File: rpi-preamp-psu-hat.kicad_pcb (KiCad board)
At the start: 2 copper layers, 41.9 x 55.9 mm, 20 parts, among them J1 Conn_02x20_Odd_Even, U1 NMH0515SC, U2 MC7809CTG

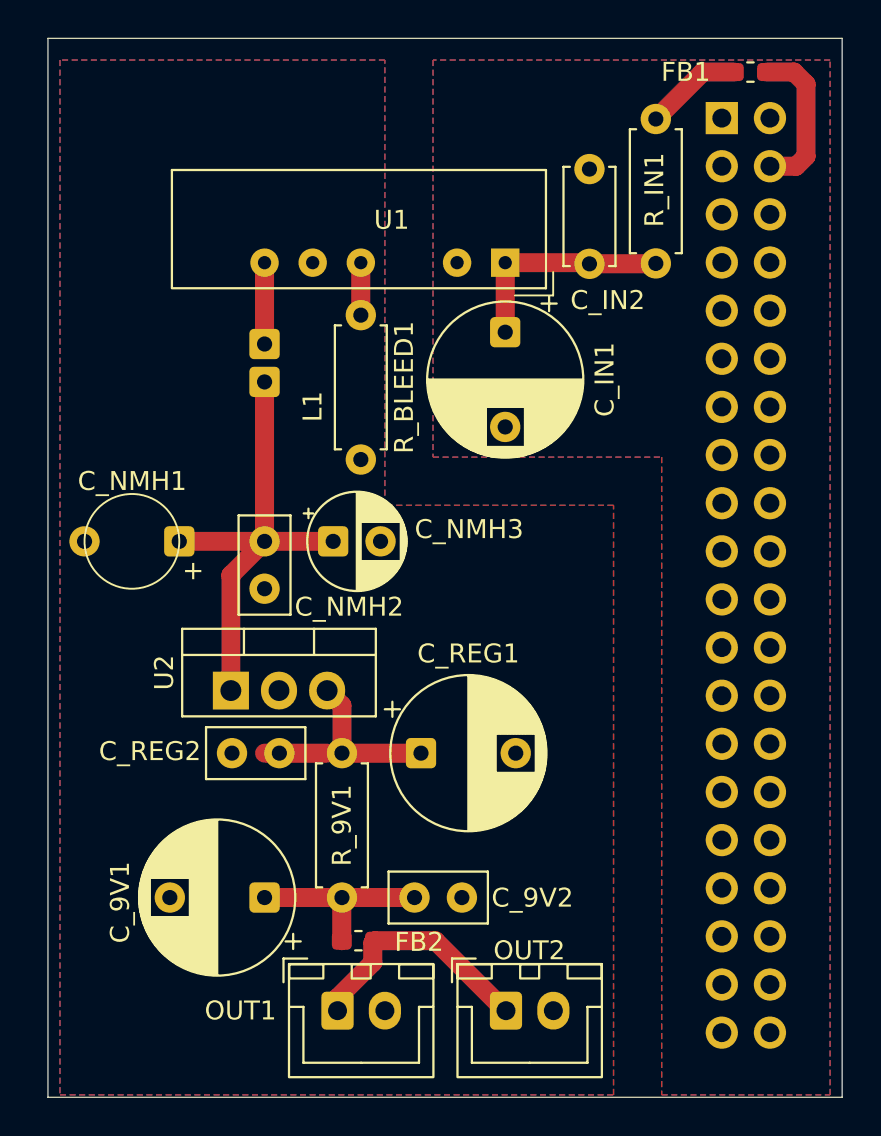
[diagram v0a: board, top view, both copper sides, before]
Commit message: Add README and a PCB tweaks
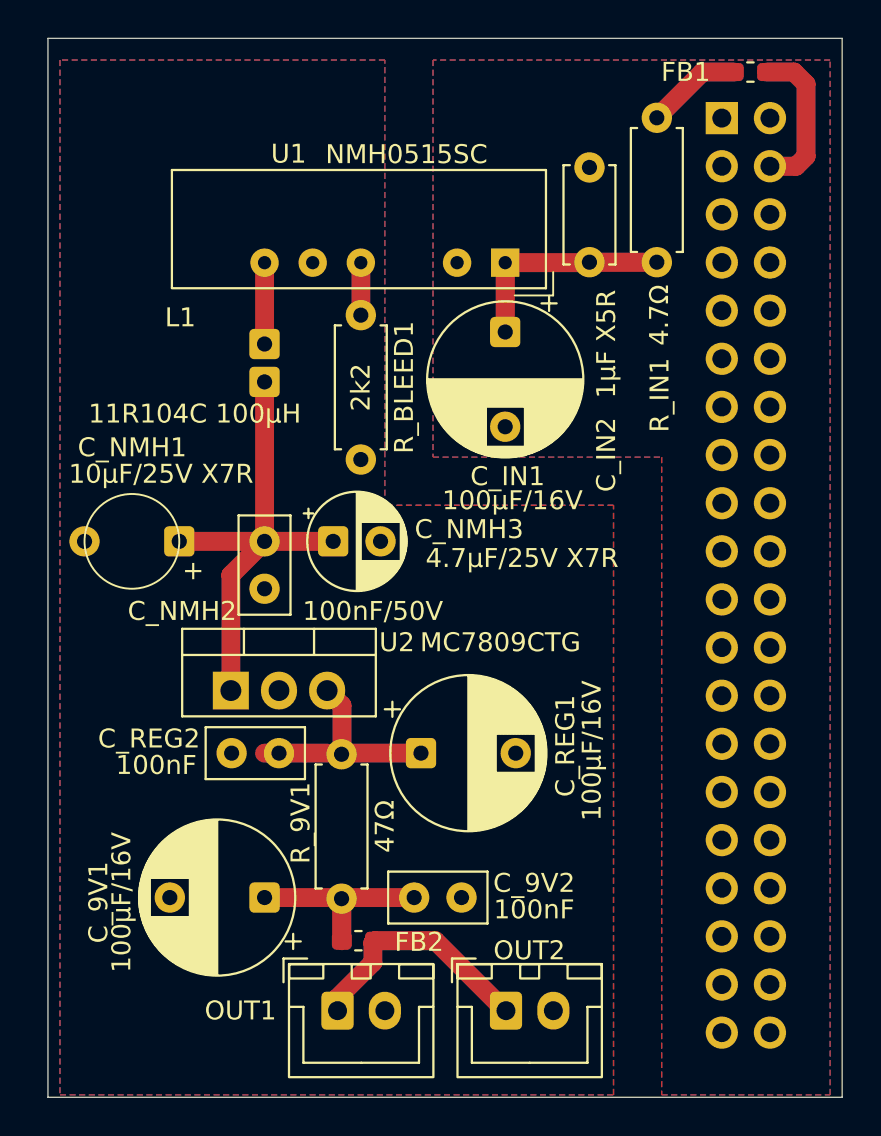
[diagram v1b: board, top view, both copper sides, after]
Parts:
- moved C_IN2 0.09 mm to (142.9, 57.7)
- moved R_IN1 0.08 mm to (146.4, 50.0)
- moved R_9V1 0.06 mm to (129.8, 83.6)
